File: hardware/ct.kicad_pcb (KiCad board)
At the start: 2 copper layers, 52.1 x 65.4 mm, 35 parts, among them J1 Banana, J2 Banana, J3 Pin Header Male, SW1 Tactile Button, U1 TLV431, U2 TLV333, U3 ATmega88PA-A

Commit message: Change U2 to MCP6V61
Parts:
- U2: value TLV333 -> MCP6V61
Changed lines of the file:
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@@
         (effects (font (size 1 1) (thickness 0.15)))
     )
-    (fp_text value "TLV333" (at 0 2.4) (layer "F.Fab")
+    (fp_text value "MCP6V61" (at 0 2.4) (layer "F.Fab")
         (effects (font (size 1 1) (thickness 0.15)))
     )

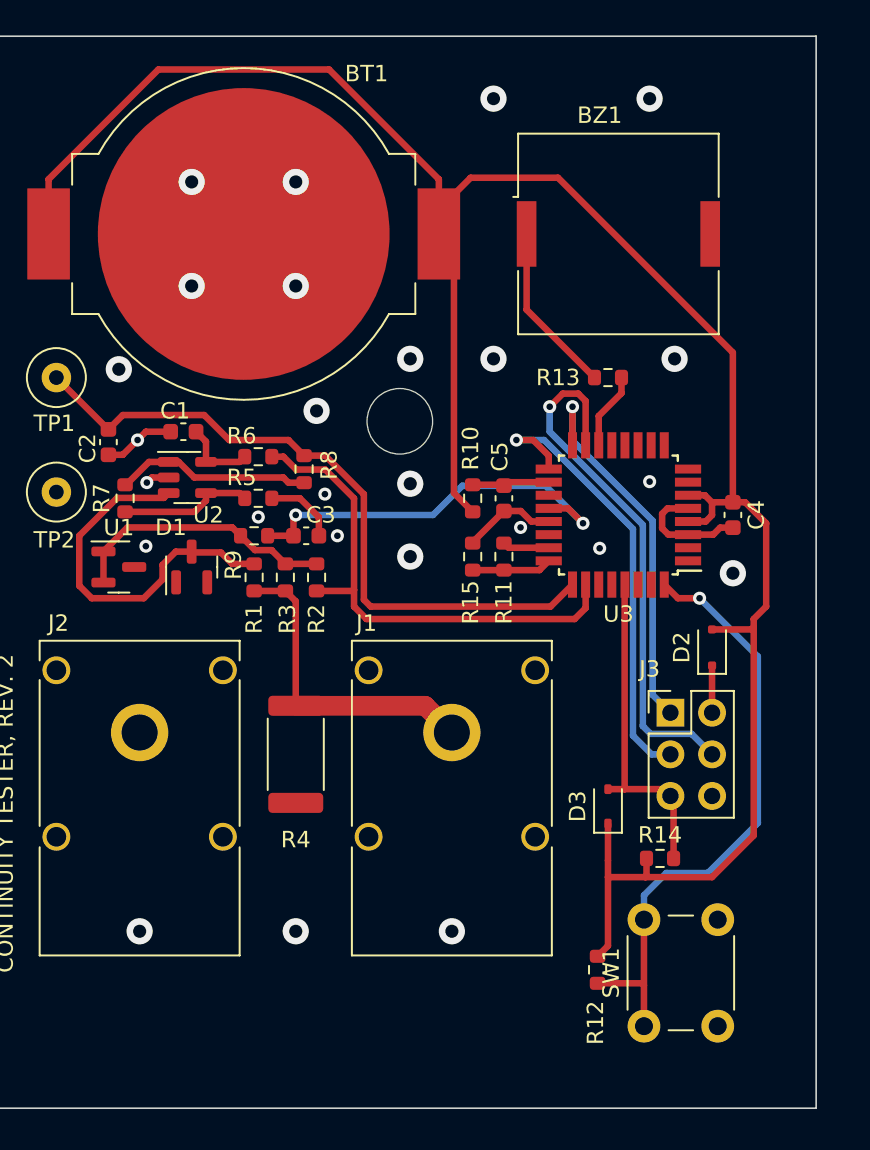
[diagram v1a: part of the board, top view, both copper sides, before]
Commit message: Add reverse polarity protection for battery
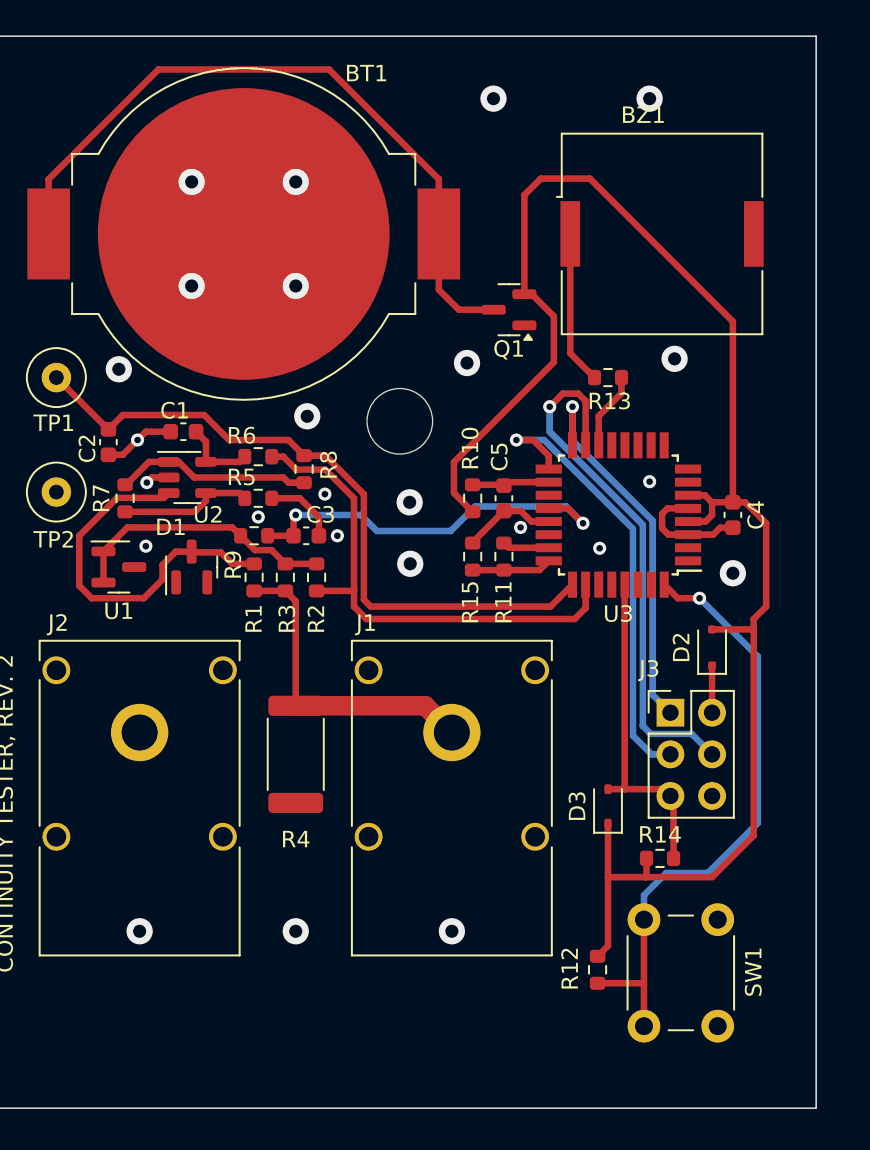
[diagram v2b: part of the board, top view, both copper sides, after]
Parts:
- added Q1: AO3423, Package_TO_SOT_SMD:SOT-23, F.Cu at (159.1, 84.0)
- moved BZ1 2.66 mm to (168.4, 79.4)
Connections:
- BT1 pad 1: VCC -> Net-(BT1-+)
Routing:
- net Net-(BT1-+): track 0.00 -> 46.1 mm
- net VCC: track 136.9 -> 100.4 mm
- net Net-(BZ1--): track 10.5 -> 9.37 mm
- net GND: vias 26 -> 25

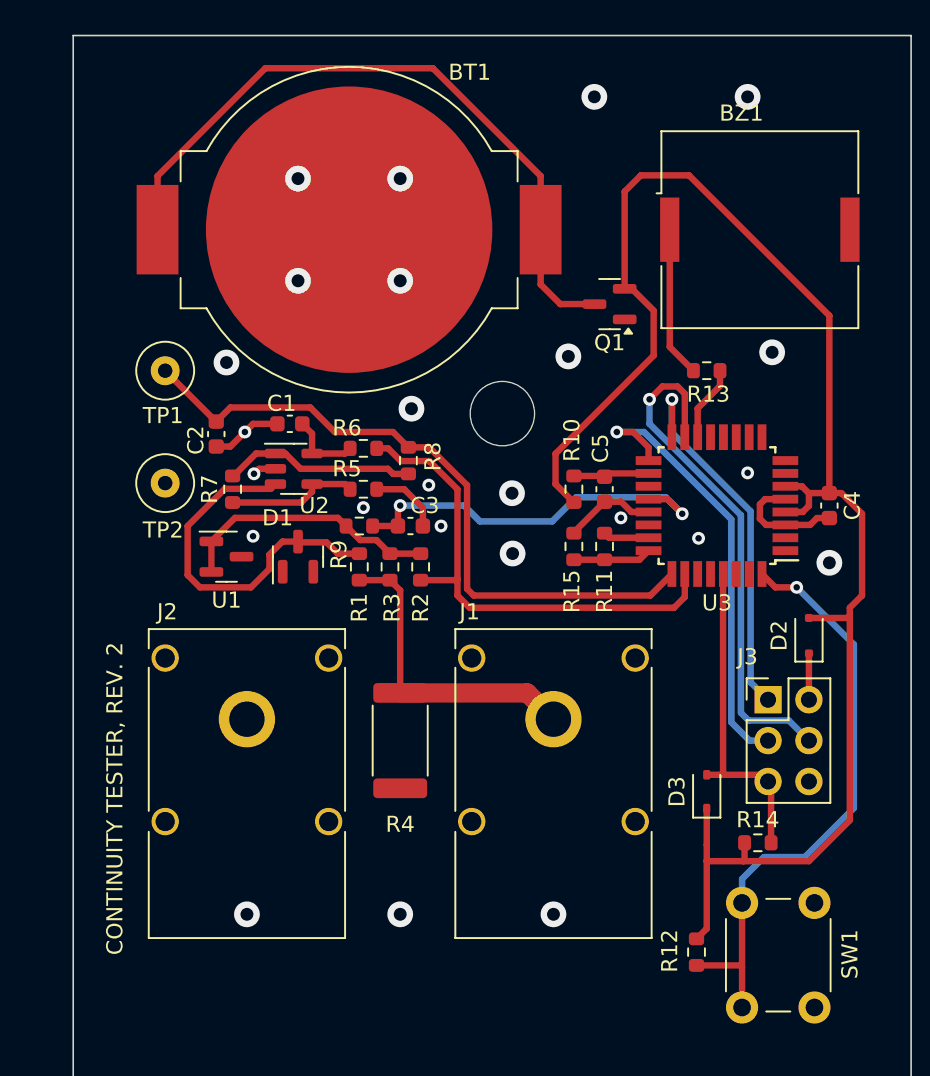
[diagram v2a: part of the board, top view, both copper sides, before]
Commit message: Add bypass to the reverse polarity protection
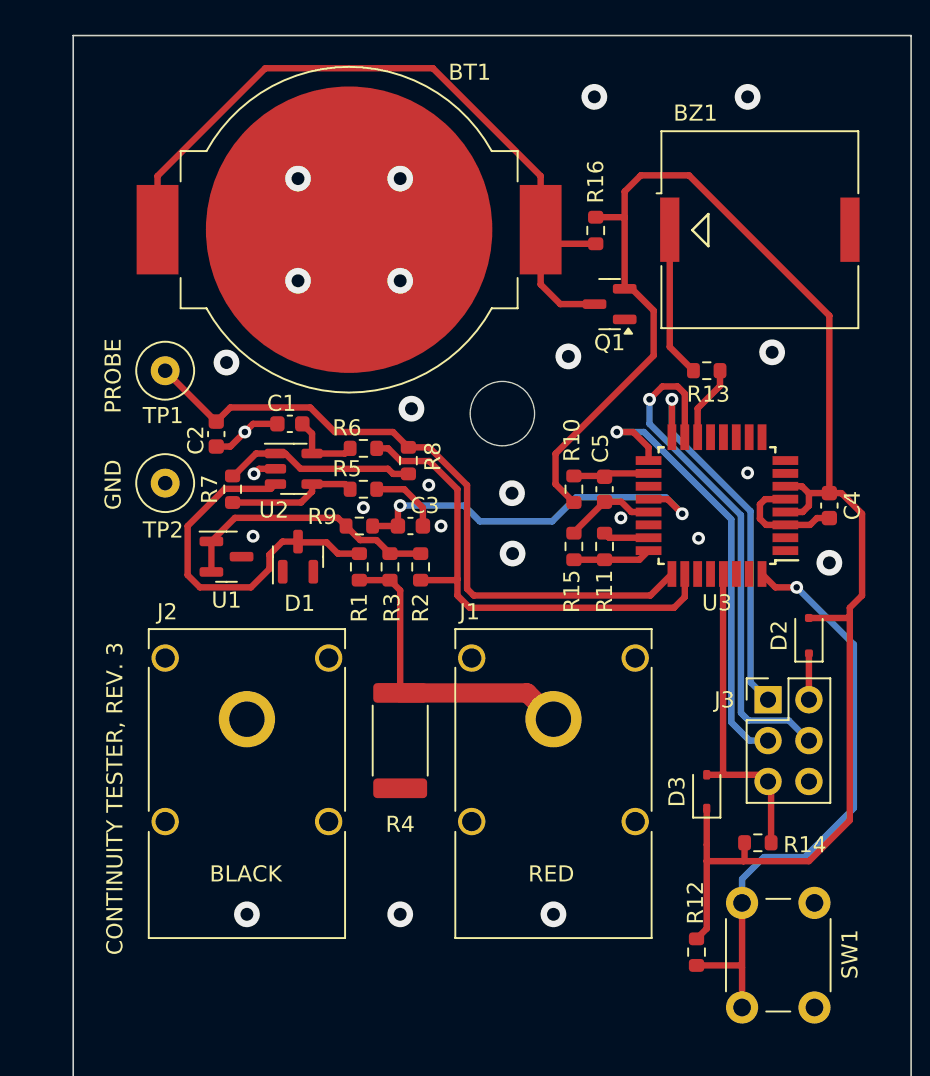
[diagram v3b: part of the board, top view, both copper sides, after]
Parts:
- added R16: 0, Resistor_SMD:R_0603_1608Metric, F.Cu at (158.2, 79.4)
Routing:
- net Net-(BT1-+): track 46.1 -> 49.9 mm
- net VCC: track 100.4 -> 102.2 mm
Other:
- board text added: "BLACK"
- board text added: "CONTINUITY TESTER, REV. 3"
- board text added: "GND"
- board text added: "PROBE"
- board text added: "RED"
- board text removed: "CONTINUITY TESTER, REV. 2"
